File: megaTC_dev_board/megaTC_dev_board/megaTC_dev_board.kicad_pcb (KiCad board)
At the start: 4 copper layers, 35 parts, among them J1 Conn_01x08_Pin, J2 Conn_01x08_Pin, J3 Conn_01x08_Pin, U1 LTC2984CLX-PBF, U2 TPD4E1B06DCKR, U3 TPD4E1B06DCKR, U4 TPD4E1B06DCKR, U5 TPD4E1B06DCKR, U6 TPD4E1B06DCKR

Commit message: routing extravaganza
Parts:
- U4, U5, U6: moved to F.Cu
- moved J3 31.4 mm to (174.3, 97.9), turned to 0 degrees
- moved J1 30.1 mm to (144.6, 97.9), turned to 0 degrees
- moved R1 28.9 mm to (171.3, 97.6), turned to -90 degrees
- moved U6 24.7 mm to (178.5, 103.8), turned to 90 degrees
- moved R2 23.8 mm to (151.8, 98.5), turned to 0 degrees
- moved U5 21.6 mm to (168.5, 108.8), turned to 90 degrees
- moved D2 21.2 mm to (151.8, 100.5), turned to 180 degrees
- moved C3 20.8 mm to (155.6, 99.4), turned to 90 degrees
- moved C2 20.4 mm to (157.3, 99.4), turned to -90 degrees
- moved C1 20.3 mm to (160.1, 99.4), turned to 90 degrees
- moved U2 20.1 mm to (147.9, 104.6), turned to -90 degrees
- moved C5 18.0 mm to (165.8, 103.2), turned to -90 degrees
- moved C14 17.9 mm to (151.8, 103.2), turned to 180 degrees
- moved J2 16.2 mm to (150.5, 121.7), turned to 90 degrees
- moved C15 15.9 mm to (151.8, 105.0), turned to 180 degrees
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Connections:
- C10 pad 1: CH12 -> CH10
- C12 pad 1: CH14 -> CH10
- C21 pad 1: CH9 -> CH10
- J2 pad 4: CH12 -> CH10
- J2 pad 6: CH14 -> CH10
- R3 pad 2: CH9 -> CH10
- R4 pad 2: CH9 -> CH10
- U1 pad 24: CH9 -> CH10
- U1 pad 27: CH12 -> CH10
- U1 pad 29: CH14 -> CH10
- U3 pad 5: CH12 -> CH10
- U4 pad 5: CH14 -> CH10
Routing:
- net CH10: track 3.81 -> 64.2 mm, vias 1 -> 6
- net CH12: track 18.5 -> 0.00 mm
- net CH14: track 15.0 -> 0.00 mm, vias 1 -> 0
- net SDO: track 14.8 -> 0.00 mm
- net RESET_LOW: track 0.53 -> 15.1 mm
- net SCK: track 13.6 -> 0.00 mm
- net INTERRUPT: track 13.5 -> 0.00 mm, vias 1 -> 0
- net CH9: track 6.08 -> 0.00 mm, vias 1 -> 0
- net CH13: track 20.3 -> 14.6 mm, vias 1 -> 2
- net SDI: track 3.57 -> 0.00 mm
- net CH15: track 13.2 -> 16.8 mm, vias 0 -> 1
- net CS_LOW: track 3.33 -> 0.00 mm
- net COMMON: track 2.52 -> 0.00 mm
- net CH11: track 15.8 -> 13.4 mm, vias 1 -> 2
- net GND: track 40.0 -> 38.8 mm, vias 25 -> 30
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
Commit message: routing done?
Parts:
- moved U6 8.26 mm to (170.2, 103.4)
- moved R1 2.74 mm to (169.2, 99.4)
- moved U5 2.15 mm to (170.2, 110.0)
- moved U4 1.64 mm to (159.5, 118.4)
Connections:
- J1 pad 1: COMMON -> GND
- J2 pad 8: GND -> COMMON
- U3 pad 4: COMMON -> CH11
- U4 pad 1: CH11 -> CH10
- U4 pad 2: CH10 -> CH13
- U4 pad 4: CH13 -> CH10
- U4 pad 5: CH10 -> CH15
- U5 pad 1: CH15 -> COMMON
- U5 pad 2: RESET_LOW -> unconnected-(U5-IO2-Pad2)
- U5 pad 4: CS_LOW -> INTERRUPT
- U5 pad 5: SDI -> SCK
- U6 pad 1: SDO -> SDI
- U6 pad 2: SCK -> SDO
- U6 pad 4: INTERRUPT -> CS_LOW
- U6 pad 5: COMMON -> RESET_LOW
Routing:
- net COMMON: track 0.00 -> 20.8 mm
- net CS_LOW: track 0.00 -> 15.1 mm
- net SDI: track 0.00 -> 14.1 mm
- net SDO: track 0.00 -> 12.9 mm
- net INTERRUPT: track 0.00 -> 11.8 mm
- net SCK: track 0.00 -> 11.8 mm
- net CH11: track 13.4 -> 23.2 mm, vias 2 -> 1
- net GND: track 38.8 -> 42.9 mm, vias 30 -> 36
- net RESET_LOW: track 15.1 -> 18.2 mm
- net CH15: track 16.8 -> 18.9 mm, vias 1 -> 2
- net CH10: track 64.2 -> 63.4 mm
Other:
- board outline added: 34.2 x 29.2 mm
- board text added: "Cu TC-RTD Dev 1 Moses Dilts 2025"
- board text removed: "Copperhead TC-RTD Dev 1 Moses Dilts 2025"

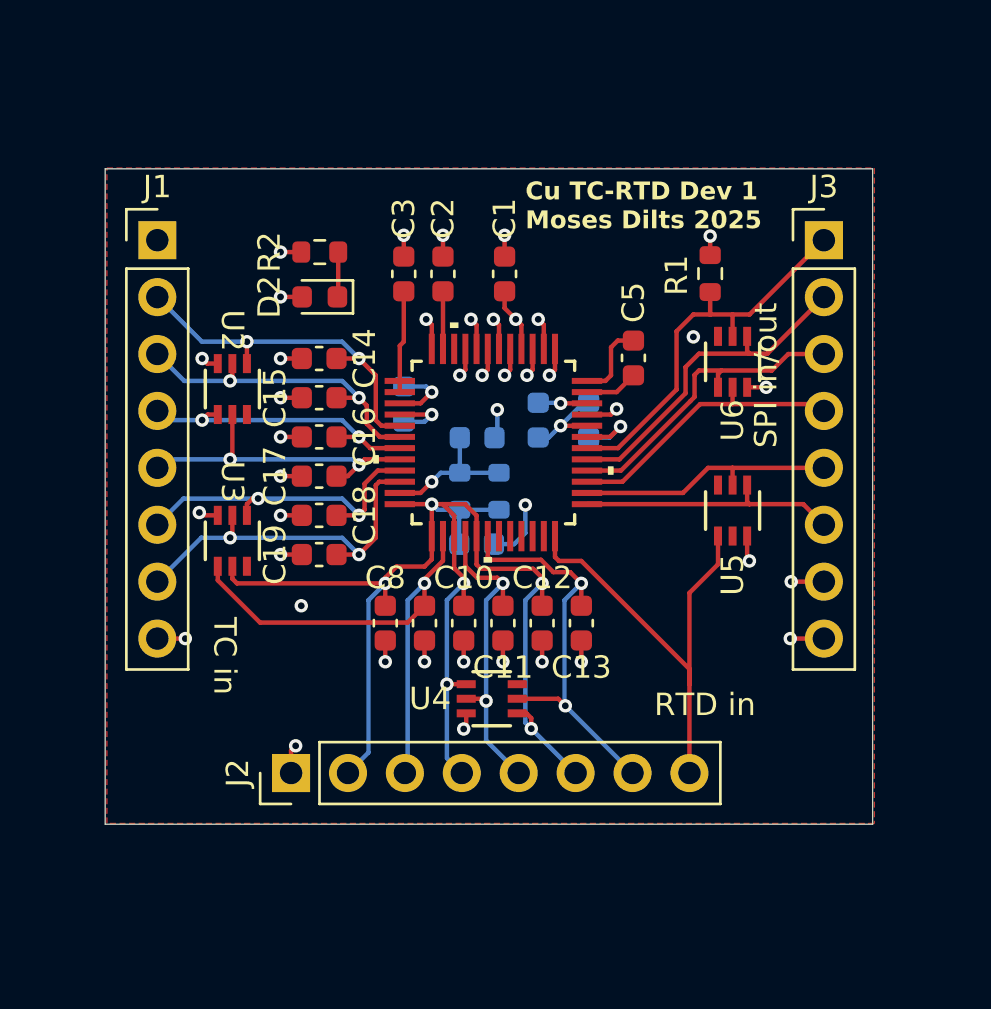
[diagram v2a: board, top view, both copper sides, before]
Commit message: added mounting holes
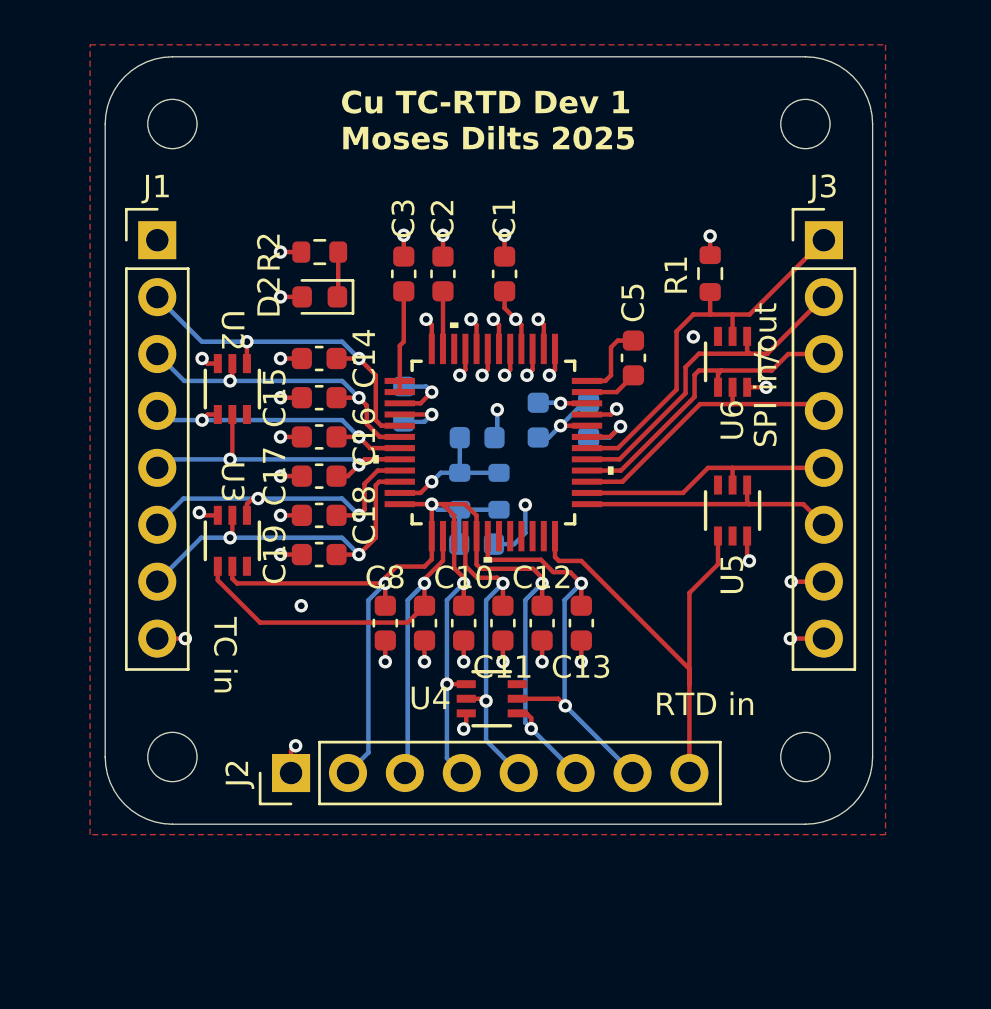
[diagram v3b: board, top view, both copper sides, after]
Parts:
- added REF**: MountingHole_2.2mm_M2_DIN965, MountingHole:MountingHole_2.2mm_M2_DIN965, F.Cu at (145.2, 92.8)
- added REF**: MountingHole_2.2mm_M2_DIN965, MountingHole:MountingHole_2.2mm_M2_DIN965, F.Cu at (145.2, 121.0)
- added REF**: MountingHole_2.2mm_M2_DIN965, MountingHole:MountingHole_2.2mm_M2_DIN965, F.Cu at (173.5, 121.0)
- added REF**: MountingHole_2.2mm_M2_DIN965, MountingHole:MountingHole_2.2mm_M2_DIN965, F.Cu at (173.5, 92.8)
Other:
- board size 34.2 x 29.2 mm -> 34.2 x 34.2 mm
- board text added: "directions: add water boil for 30 mins serve"
